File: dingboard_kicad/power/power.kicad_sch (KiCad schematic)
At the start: 0 parts

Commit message: add reference step file from kicad PCIe
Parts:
- added J1: Bus_PCI_Express_x1, Connector_PCBEdge:BUS_PCIexpress_x1, symbol Connector:Bus_PCI_Express_x1
- added U1: RP2040, Package_DFN_QFN:QFN-56-1EP_7x7mm_P0.4mm_EP3.2x3.2mm, symbol MCU_RaspberryPi:RP2040
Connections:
- new net: U1.1 (IOVDD), U1.10 (IOVDD), U1.22 (IOVDD), U1.33 (IOVDD), U1.42 (IOVDD), U1.49 (IOVDD)
- new net: U1.23 (DVDD), U1.50 (DVDD)
- new net: J1.A10 (+3.3V), J1.A9 (+3.3V), J1.B8 (+3.3V)
- new net: J1.A12 (GND), J1.A15 (GND), J1.A18 (GND), J1.A4 (GND), J1.B13 (GND), J1.B16 (GND), J1.B18 (GND), J1.B4 (GND), J1.B7 (GND)
- new net: J1.A2 (+12V), J1.A3 (+12V), J1.B1 (+12V), J1.B2 (+12V), J1.B3 (+12V)

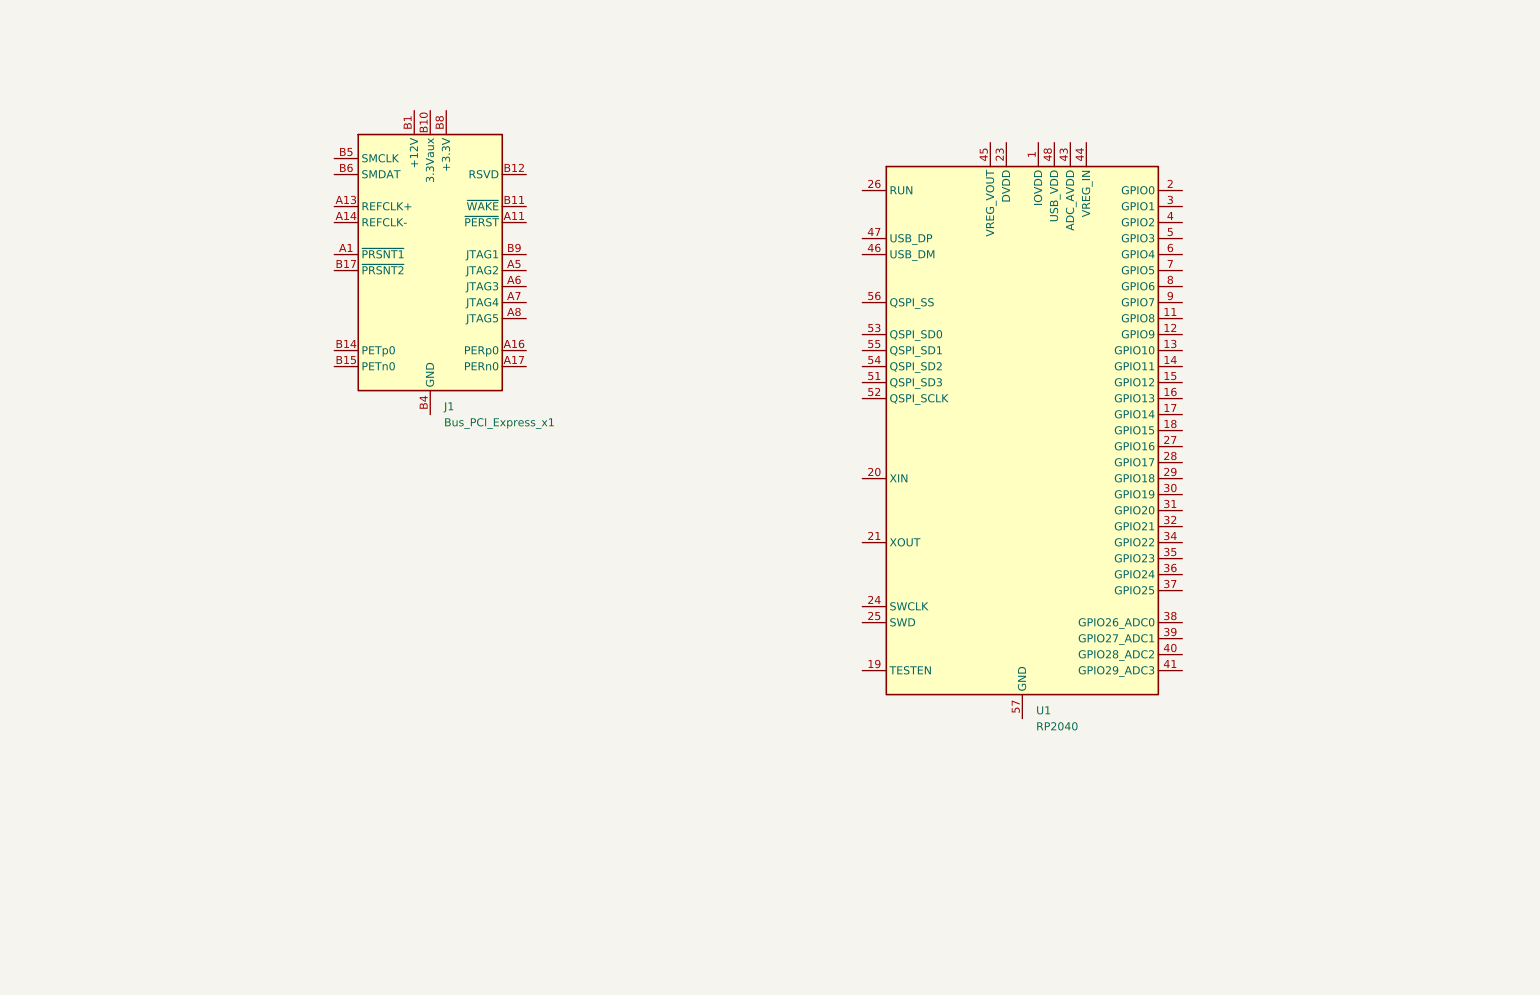
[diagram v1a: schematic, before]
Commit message: add components to kicad power module
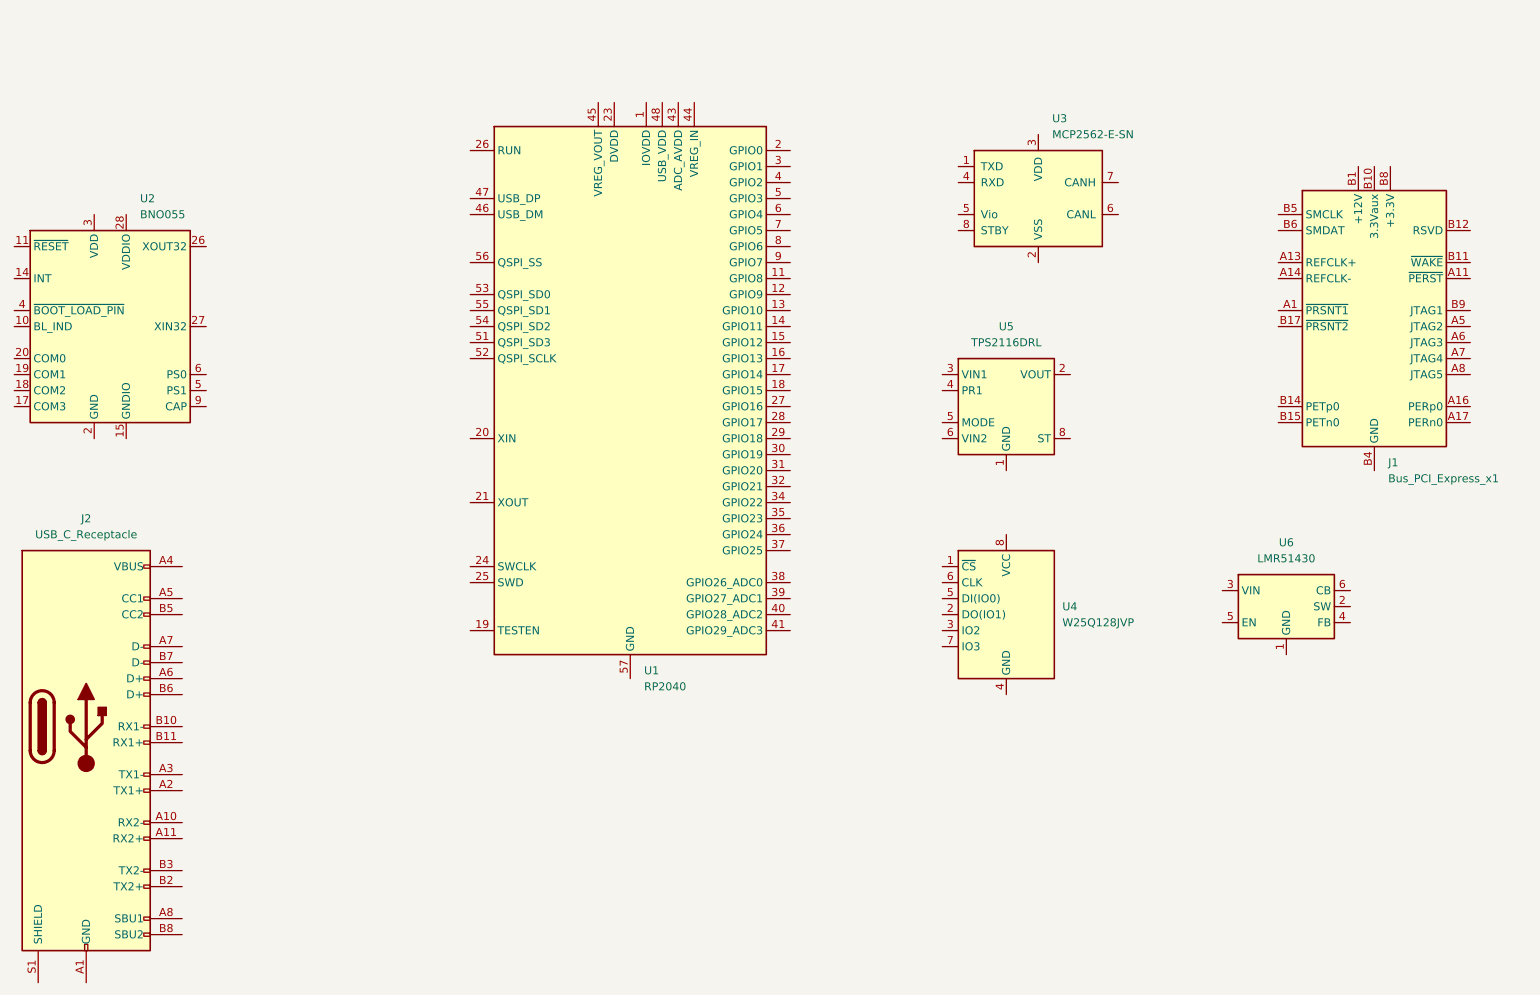
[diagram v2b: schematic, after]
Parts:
- added J2: USB_C_Receptacle, Connector_USB:USB_C_Receptacle_Amphenol_12401548E4-2A, symbol Connector:USB_C_Receptacle
- added U2: BNO055, Package_LGA:LGA-28_5.2x3.8mm_P0.5mm, symbol Sensor_Motion:BNO055
- added U3: MCP2562-E-SN, Package_SO:SOIC-8_3.9x4.9mm_P1.27mm, symbol Interface_CAN_LIN:MCP2562-E-SN
- added U4: W25Q128JVP, Package_SON:WSON-8-1EP_6x5mm_P1.27mm_EP3.4x4.3mm, symbol Memory_Flash:W25Q128JVP
- added U5: TPS2116DRL, Package_TO_SOT_SMD:SOT-583-8, symbol Power_Management:TPS2116DRL
- added U6: LMR51430, Package_TO_SOT_SMD:SOT-23-6, symbol Regulator_Switching:LMR51430
- J1: LCSC (none) -> n/a; basic? (none) -> n/a; jlc link (none) -> n/a; price (none) -> n/a
- U1: LCSC (none) -> C2040 Copy; basic? (none) -> no; jlc link (none) -> https://jlcpcb.com/parts/componentSearch?searchTxt=rp2040; price (none) -> C$1.4190
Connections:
- new net: U2.15 (GNDIO), U2.16 (GNDIO), U2.25 (GNDIO)
- new net: U5.2 (VOUT), U5.7 (VOUT)
- new net: J2.A1 (GND), J2.A12 (GND), J2.B1 (GND), J2.B12 (GND)
- new net: J2.A4 (VBUS), J2.A9 (VBUS), J2.B4 (VBUS), J2.B9 (VBUS)
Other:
- moved on the sheet: J1, U1

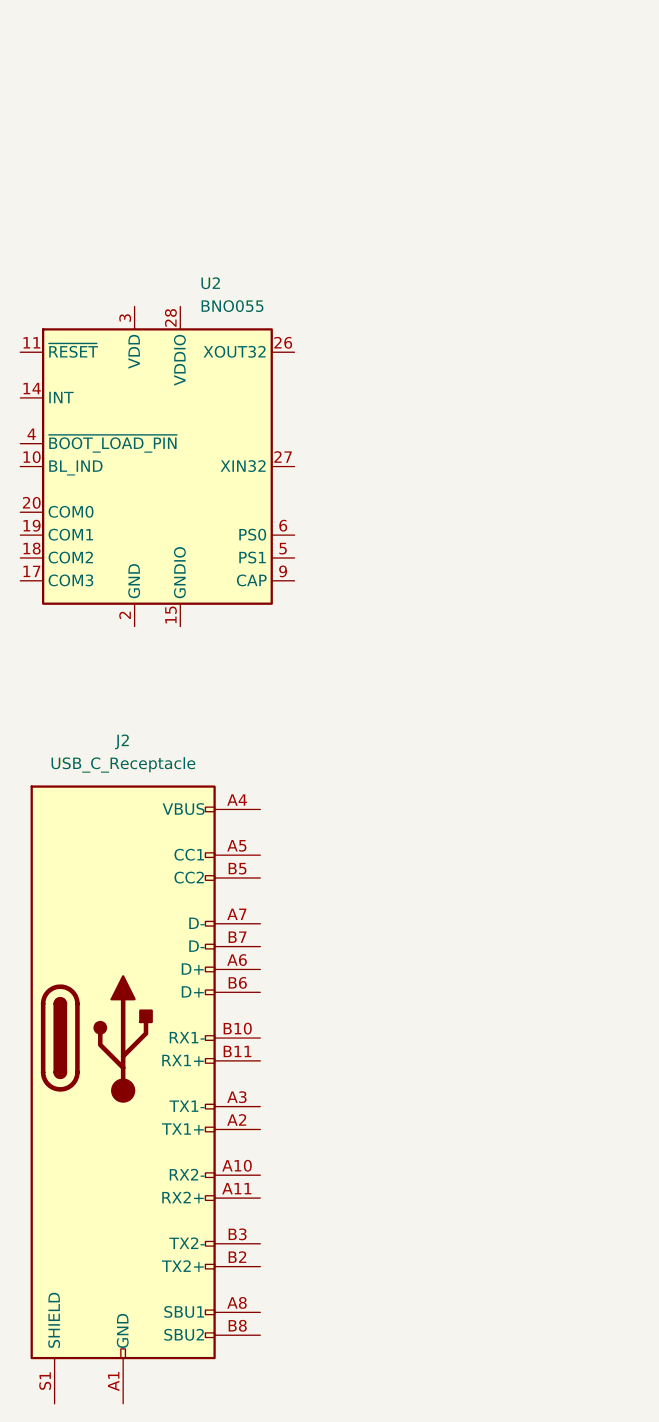
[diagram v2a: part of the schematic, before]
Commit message: create kicad template
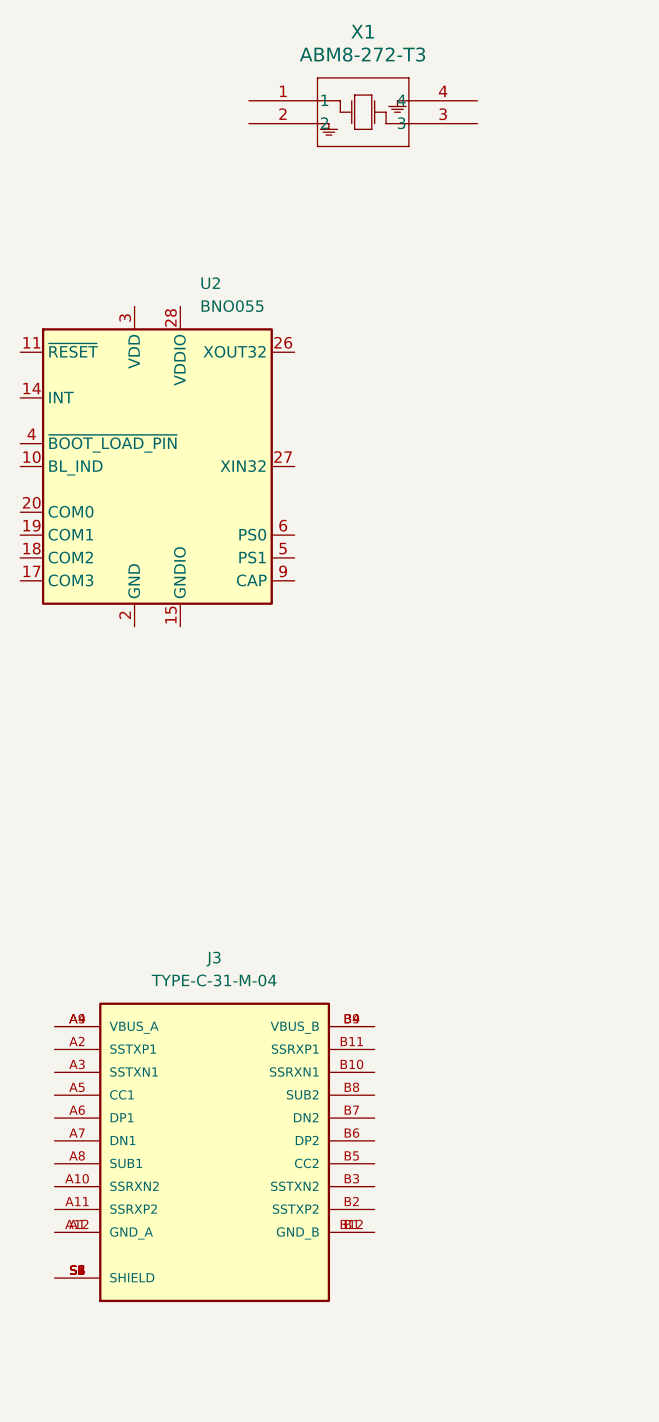
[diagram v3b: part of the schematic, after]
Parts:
- removed J2: USB_C_Receptacle, Connector_USB:USB_C_Receptacle_Amphenol_12401548E4-2A, symbol Connector:USB_C_Receptacle
- added J3: TYPE-C-31-M-04, TYPE-C-31-M-04:HRO_TYPE-C-31-M-04, symbol TYPE-C-31-M-04:TYPE-C-31-M-04
- added X1: ABM8-272-T3, footprints:ABM8-272-T3_ABR, symbol 2024-12-09_07-34-56:ABM8-272-T3
- J1: jlc link n/a -> (none); link (none) -> n/a
- U1: LCSC C2040 Copy -> C2040; jlc link https://jlcpcb.com/parts/componentSearch?searchTxt=rp2040 -> (none); link (none) -> https://jlcpcb.com/parts/componentSearch?searchTxt=rp2040
- U2: jlc link https://jlcpcb.com/partdetail/BoschSensortec-BNO055/C93216 -> (none); link (none) -> https://jlcpcb.com/partdetail/BoschSensortec-BNO055/C93216
- U4: jlc link https://jlcpcb.com/partdetail/WinbondElec-W25Q128JVPIQ/C190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 -> (none); link (none) -> https://jlcpcb.com/partdetail/WinbondElec-W25Q128JVPIQ/C190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
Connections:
- new net: J3.A1 (GND_A), J3.A12 (GND_A)
- new net: J3.A4 (VBUS_A), J3.A9 (VBUS_A)
- new net: J3.B1 (GND_B), J3.B12 (GND_B)
- new net: J3.B4 (VBUS_B), J3.B9 (VBUS_B)
- new net: J3.S1 (SHIELD), J3.S2 (SHIELD), J3.S3 (SHIELD), J3.S4 (SHIELD), J3.S5 (SHIELD), J3.S6 (SHIELD), J3.S7 (SHIELD), J3.S8 (SHIELD)
